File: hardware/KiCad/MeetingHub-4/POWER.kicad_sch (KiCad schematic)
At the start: 6 parts, among them J1 USB-C POWER IN

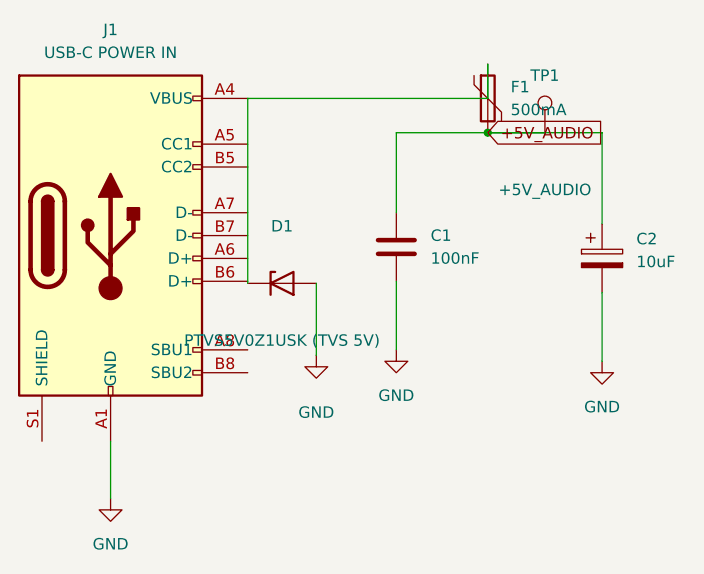
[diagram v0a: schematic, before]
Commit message: Add PCB layout with all 70 footprints placed, fix outline and clearance
Board now has all components placed (from Update PCB from Schematic +
manual arrangement), a closed rectangular Edge.Cuts outline sized around
the component bounding box, and the Default netclass clearance relaxed
from 0.2mm to 0.15mm to match the USB-C connector's fine pin pitch.

Removed a stray Edge.Cuts reference line baked into the RK097 potentiometer
footprint (5 instances) that was preventing outline closure - it's a
library alignment artifact, not a real board cutout, so this is an
intentional local deviation from the library copy (shows up as a harmless
lib_footprint_mismatch warning in DRC).

DRC is clean of errors: 0 outline/clearance violations. Remaining silk
overlap warnings are cosmetic (deferred to final placement polish per
PCB-001) and the 143 unconnected-pad errors are expected pre-routing
ratsnest, not yet addressed (routing is next).

Co-Authored-By: Claude Sonnet 5 <noreply@anthropic.com>
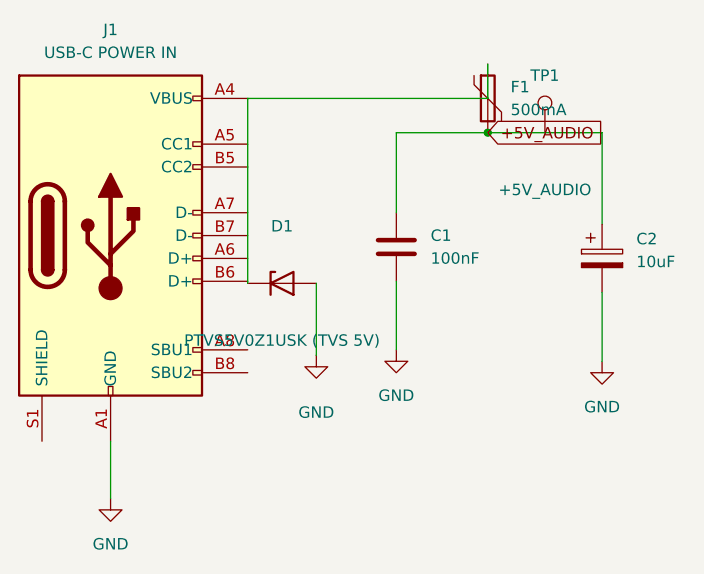
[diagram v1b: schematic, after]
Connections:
- net +5V_AUDIO: no longer TP1.1

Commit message: Fix real ERC errors: TP1 never connected, U1 power_pin_not_driven, stale AudioJack4 lib_id
- POWER.kicad_sch: add missing junction so TP1 actually joins the
  +5V_AUDIO wire (visual overlap without a junction is not a real
  connection in KiCad); add two power:PWR_FLAG symbols (+5V_AUDIO, GND)
  so ERC has an explicit power source for nets fed only by J1's USB-C
  VBUS pin, resolving power_pin_not_driven on U1.
- MeetingHub-4.kicad_pcb: TP1's pad had no net at all on the physical
  board (unconnected-(TP1-Pad1)), and TP2 (GND test point added
  directly on the PCB) had no net either - both test points were
  floating on the real board despite BOM/docs claiming otherwise. Fixed
  by assigning TP1 to +5V_AUDIO and TP2 to GND, then refilling the
  internal planes so the pads actually bond to them. Verified 0
  unconnected items and 0 real DRC errors after the fix.
- TRRS.kicad_sch: J2-J6 referenced Connector:AudioJack4, a library path
  that no longer exists in current KiCad (symbol moved to
  Connector_Audio) - only worked because of the cached copy. Repointed
  lib_id to Connector_Audio:AudioJack4 after confirming the cached
  symbol is byte-identical to the current system library version.

Found while working through the user's real GUI ERC report (248
messages). Documented in PCB-001 Fase 11 and BOM-002-AsBuilt Seção 4.

Co-Authored-By: Claude Sonnet 5 <noreply@anthropic.com>
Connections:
- net +5V_AUDIO: now also TP1.1
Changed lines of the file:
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@@
     (stroke (width 0) (type default))
+  )
+  (junction (at 95.25 48.26) (diameter 0) (color 0 0 0 0)
+  )
+  (junction (at 75.565 44.45) (diameter 0) (color 0 0 0 0)
+  )
+  (junction (at 69.85 69) (diameter 0) (color 0 0 0 0)
+  )
+  (symbol (lib_id "power:PWR_FLAG") (at 75.565 44.45 0) (unit 1)
+    (in_bom yes) (on_board yes) (dnp no)
+    (property "Reference" "#FLG01" (at 75.565 46.355 0)
+      (effects (font (size 1.27 1.27)) hide)
+    )
+    (property "Value" "PWR_FLAG" (at 75.565 48.26 0)
+      (effects (font (size 1.27 1.27)))
+    )
+    (property "Footprint" "" (at 75.565 44.45 0)
+      (effects (font (size 1.27 1.27)) hide)
+    )
+    (property "Datasheet" "~" (at 75.565 44.45 0)
+      (effects (font (size 1.27 1.27)) hide)
+    )
+    (instances
+      (project "MeetingHub-4"
+        (path "/8b7deae6-c6d2-463d-9623-40608a842bd8/7adc5442-2532-4675-a48f-0351bbf6b21b"
+          (reference "#FLG01") (unit 1)
+        )
+      )
+    )
+  )
+  (symbol (lib_id "power:PWR_FLAG") (at 69.85 69 90) (unit 1)
+    (in_bom yes) (on_board yes) (dnp no)
+    (property "Reference" "#FLG02" (at 67.945 69 90)
+      (effects (font (size 1.27 1.27)) hide)
+    )
+    (property "Value" "PWR_FLAG" (at 66.04 69 90)
+      (effects (font (size 1.27 1.27)))
+    )
+    (property "Footprint" "" (at 69.85 69 90)
+      (effects (font (size 1.27 1.27)) hide)
+    )
+    (property "Datasheet" "~" (at 69.85 69 90)
+      (effects (font (size 1.27 1.27)) hide)
+    )
+    (instances
+      (project "MeetingHub-4"
+        (path "/8b7deae6-c6d2-463d-9623-40608a842bd8/7adc5442-2532-4675-a48f-0351bbf6b21b"
+          (reference "#FLG02") (unit 1)
+        )
+      )
+    )
   )
   (wire (pts (xy 88.9 48.26) (xy 101.6 48.26))

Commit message: Fix remaining ERC errors: wrong PWR_FLAG net, missing no-connects, J6 AudioJack4
- POWER.kicad_sch: relocate #FLG01 (+5V_AUDIO PWR_FLAG) - it was tapped
  on the wire feeding fuse F1 from the input side, not the actual
  +5V_AUDIO net downstream of F1 (same node as TP1 and the +5V_AUDIO
  global label). U1 Pin 8 (V+) kept reporting power_pin_not_driven
  because of this even after the first fix. Also add no_connect markers
  on J1's 9 unused USB-C pins (D+, D-, CC1, CC2, SBU1, SBU2, SHIELD) -
  intentional since J1 is power-only, but ERC flagged them as errors
  without an explicit no-connect.
- MICSW.kicad_sch: add no_connect on K1-K4 pin 10 (duplicate reverse
  relay contact, unused in this SPDT wiring) - same reasoning, silences
  a real ERC error instead of just being documented as expected.
- HPAMP.kicad_sch: J6 also referenced the stale Connector:AudioJack4
  lib_id (missed in the previous fix, which only covered J2-J5 in
  TRRS.kicad_sch). Repointed to Connector_Audio:AudioJack4.

Found from the user's second real ERC report after the previous round
of fixes. Documented in PCB-001 Fase 11 and BOM-002-AsBuilt Seção 4.

Co-Authored-By: Claude Sonnet 5 <noreply@anthropic.com>
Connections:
- no-connect marks 0 -> 9
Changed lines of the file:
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@@
   (junction (at 95.25 48.26) (diameter 0) (color 0 0 0 0)
   )
-  (junction (at 75.565 44.45) (diameter 0) (color 0 0 0 0)
+  (junction (at 83.325 48.26) (diameter 0) (color 0 0 0 0)
   )
   (junction (at 69.85 69) (diameter 0) (color 0 0 0 0)
   )
-  (symbol (lib_id "power:PWR_FLAG") (at 75.565 44.45 0) (unit 1)
+  (no_connect (at 62.23 49.53))
+  (no_connect (at 62.23 52.07))
+  (no_connect (at 62.23 57.15))
+  (no_connect (at 62.23 59.69))
+  (no_connect (at 62.23 62.23))
+  (no_connect (at 62.23 64.77))
+  (no_connect (at 62.23 72.39))
+  (no_connect (at 62.23 74.93))
+  (no_connect (at 39.37 82.55))
+  (symbol (lib_id "power:PWR_FLAG") (at 83.325 48.26 0) (unit 1)
     (in_bom yes) (on_board yes) (dnp no)
-    (property "Reference" "#FLG01" (at 75.565 46.355 0)
+    (property "Reference" "#FLG01" (at 83.325 50.165 0)
       (effects (font (size 1.27 1.27)) hide)
     )
-    (property "Value" "PWR_FLAG" (at 75.565 48.26 0)
+    (property "Value" "PWR_FLAG" (at 83.325 52.07 0)
       (effects (font (size 1.27 1.27)))
     )
-    (property "Footprint" "" (at 75.565 44.45 0)
+    (property "Footprint" "" (at 83.325 48.26 0)
       (effects (font (size 1.27 1.27)) hide)
     )
-    (property "Datasheet" "~" (at 75.565 44.45 0)
+    (property "Datasheet" "~" (at 83.325 48.26 0)
       (effects (font (size 1.27 1.27)) hide)
     )
